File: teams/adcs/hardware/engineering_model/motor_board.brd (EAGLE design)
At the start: 90 x 90 mm, 63 parts

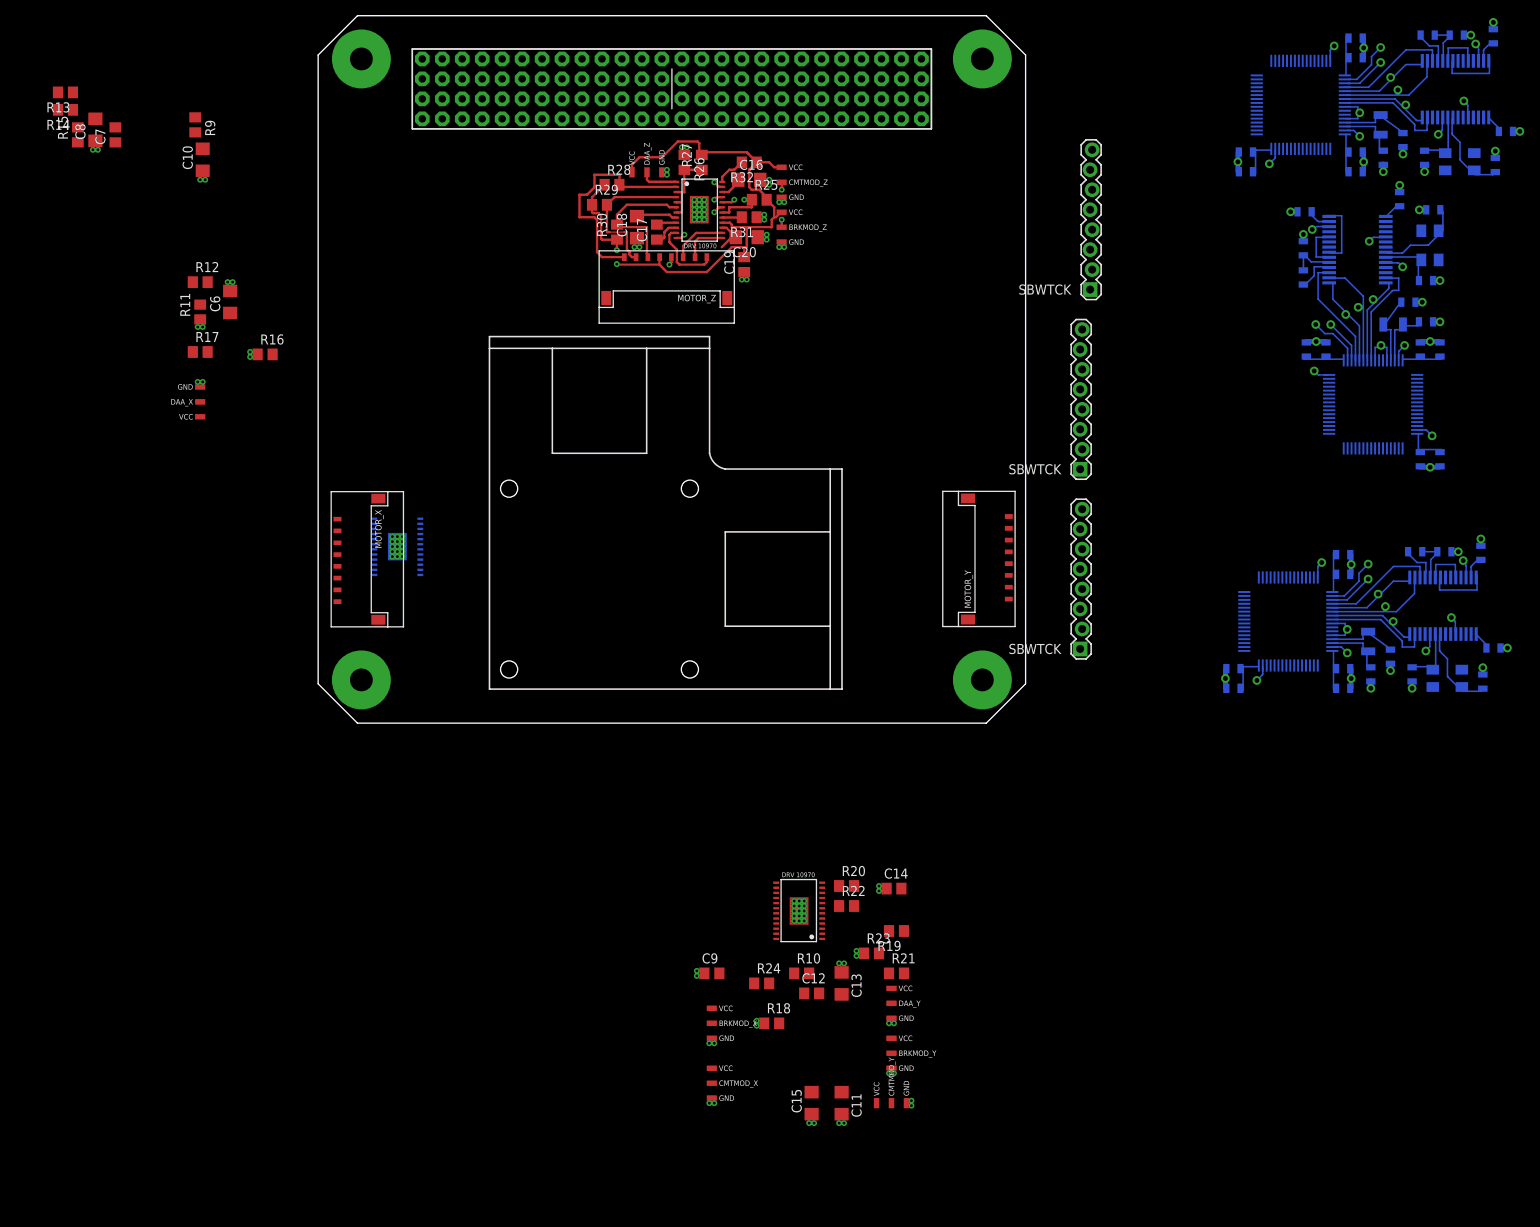
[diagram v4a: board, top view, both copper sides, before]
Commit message: ADCS/RW: Utilize design block in further routing progress
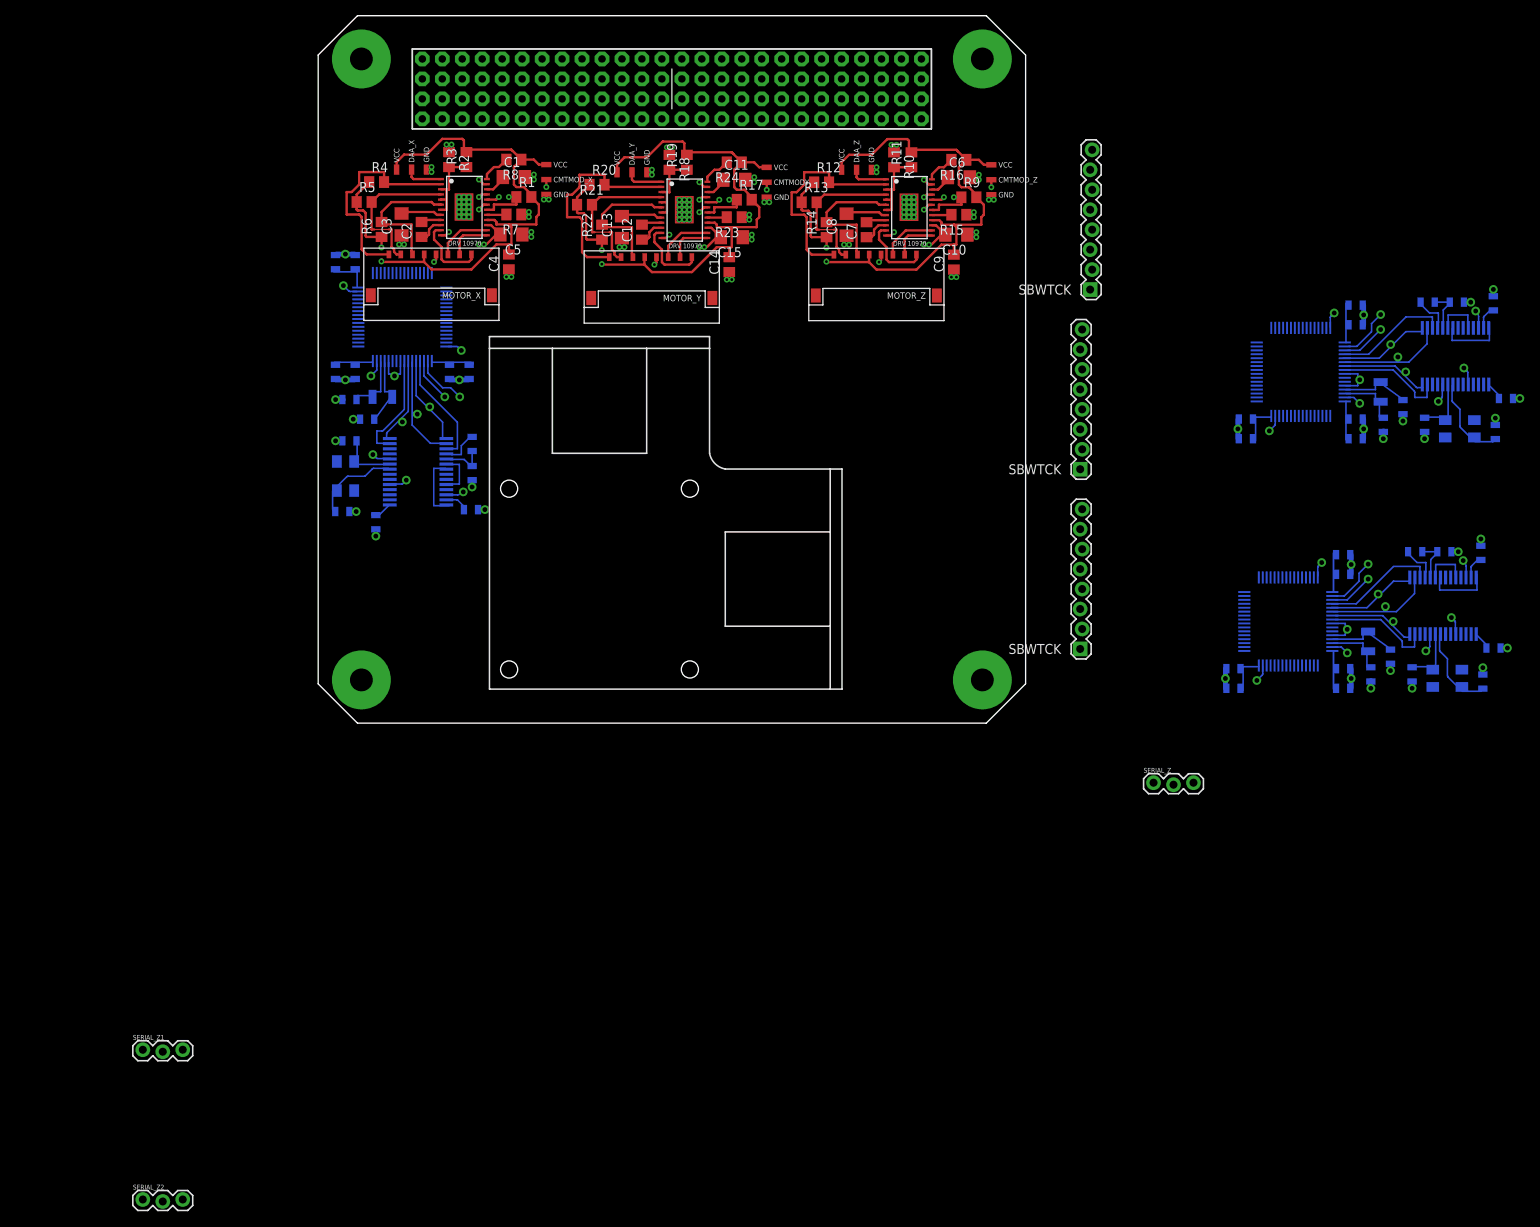
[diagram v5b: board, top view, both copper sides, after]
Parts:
- removed BRKMOD_X, BRKMOD_Y, BRKMOD_Z, CMTMOD_Y: 0_OHM_JUMPER, DubSat1 Components:0_OHM_JUMPER
- removed C16: 2.2uF, rcl:C1206
- removed C17, C19: 0.1uF, rcl:C0805
- removed C18, C20: 1uF, rcl:C1206
- removed R25, R26, R27, R32: 3.3K, rcl:R0805
- removed R28, R29, R30: 10K, rcl:R0805
- removed R31: (no value), rcl:R0805
- removed U$12: DRV10970, DubSat1 Components:DRV10970
- added C1: 2.2uF, rcl:C1206
- added C2, C4: 0.1uF, rcl:C0805
- added C3, C5: 1uF, rcl:C1206
- added CMTMODY: 0_OHM_JUMPER, DubSat1 Components:0_OHM_JUMPER
- added R1, R2, R3, R8: 3.3K, rcl:R0805
- added R4, R5, R6: 10K, rcl:R0805
- added R7: (no value), rcl:R0805
- added SERIAL_Z, SERIAL_Z1, SERIAL_Z2: (no value), SparkFun-Connectors:1X03_LOCK
- added U$13: DRV10970, DubSat1 Components:DRV10970
- R12: value 3.3K -> 10K
- R15: value 10K -> (none)
- R16: value (none) -> 3.3K
- moved C11 118.3 mm to (53.7, 69.8), turned to 0 degrees
- moved U$3 117.4 mm to (11.4, 52.4), turned to 180 degrees
- moved CMTMOD_X 116.9 mm to (29.7, 69.9)
- moved R15 112.5 mm to (82.2, 65.4), turned to 180 degrees
- moved DAA_Y 110.8 mm to (40.6, 70.8), turned to 90 degrees
- moved C15 110.6 mm to (53.3, 62.5), turned to 180 degrees
- moved R18 110.3 mm to (45.4, 72.1), turned to 270 degrees
- moved R21 105.5 mm to (34.6, 66.7)
- moved R24 104.5 mm to (53.7, 72.1), turned to 180 degrees
- moved R10 104.2 mm to (74.0, 72.4), turned to 270 degrees
- moved R19 101.4 mm to (47.6, 72.1), turned to 90 degrees
- moved C13 100.2 mm to (39.4, 63.8), turned to 90 degrees
- moved C12 99.2 mm to (41.9, 63.2), turned to 90 degrees
- moved U$7 99.2 mm to (19.3, 66.4), turned to 270 degrees
- moved R9 98.9 mm to (83.5, 67.6), turned to 0 degrees
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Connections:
- net N$20 renamed RETRY_Z
- net N$24 renamed VCP_Z
- net N$50 renamed CPP_Z
- net N$51 renamed CPN_Z
- removed net N$13: C11.1, U$7.RETRY
- removed net N$14: C13.2, U$7.VCP
- removed net N$15: R18.2, R19.1, U$7.U_HN, U$7.V_HN, U$7.W_HN
- removed net N$16: DAA_Y.P$2, U$7.DAA
- removed net N$17: CMTMOD_Y.P$2, U$7.CMTMOD
- removed net N$18: BRKMOD_Y.P$2, U$7.BRKMOD
- removed net N$21: C12.2, U$7.CPP
- removed net N$22: C12.1, U$7.CPN
- removed net N$23: MOTOR_Y.P$1, U$7.W
- removed net N$25: MOTOR_Y.P$2, U$7.V
- removed net N$30: R11.2, R12.1, U$10.U_HN, U$10.V_HN, U$10.W_HN
- removed net N$36: DAA_X.P$2, U$10.DAA
- removed net N$38: CMTMOD_X.P$2, U$10.CMTMOD
- removed net N$39: BRKMOD_X.P$2, U$10.BRKMOD
- removed net N$40: MOTOR_Y.P$6, R22.2, U$7.W_HP
- removed net N$41: MOTOR_Y.P$7, R21.2, U$7.V_HP
- removed net N$52: MOTOR_X.P$1, U$10.W
- removed net N$53: MOTOR_X.P$2, U$10.V
- removed net N$54: MOTOR_X.P$6, R15.2, U$10.W_HP
- removed net N$55: MOTOR_X.P$7, R14.2, U$10.V_HP
- removed net N$57: MOTOR_X.P$8, R13.2, U$10.U_HP
- removed net N$58: R16.2, U$10.CS
- removed net N$59: MOTOR_X.P$3, U$10.U
- removed net N$60: MOTOR_Y.P$8, R20.2, U$7.U_HP
- removed net N$61: R23.2, U$7.CS
- removed net N$62: MOTOR_Y.P$3, U$7.U
- removed net N$69: C16.1, U$12.RETRY
- removed net N$70: C18.2, U$12.VCP
- removed net N$71: R26.2, R27.1, U$12.U_HN, U$12.V_HN, U$12.W_HN
- removed net N$72: DAA_Z.P$2, U$12.DAA
- removed net N$73: CMTMOD_Z.P$2, U$12.CMTMOD
- removed net N$74: BRKMOD_Z.P$2, U$12.BRKMOD
- removed net N$75: C17.2, U$12.CPP
- removed net N$76: C17.1, U$12.CPN
- removed net N$77: MOTOR_Z.P$1, U$12.W
- removed net N$78: MOTOR_Z.P$2, U$12.V
- removed net N$79: MOTOR_Z.P$6, R30.2, U$12.W_HP
- removed net N$80: MOTOR_Z.P$7, R29.2, U$12.V_HP
- removed net N$81: MOTOR_Z.P$8, R28.2, U$12.U_HP
- removed net N$82: R31.2, U$12.CS
- removed net N$83: MOTOR_Z.P$3, U$12.U
- removed net VM_X: C10.2, U$10.VM
- removed net VM_Y: C15.2, U$7.VM
- new net BRKMOD_X: U$7.BRKMOD
- new net BRKMOD_Y: U$13.BRKMOD
- new net BRKMOD_Z: U$10.BRKMOD
- new net CMTMOD_X: CMTMOD_X.P$2, U$7.CMTMOD
- new net CMTMOD_Y: CMTMODY.P$2, U$13.CMTMOD
- new net CMTMOD_Z: CMTMOD_Z.P$2, U$10.CMTMOD
- new net CPN_X: C2.1, U$7.CPN
- new net CPN_Y: C12.1, U$13.CPN
- new net CPP_X: C2.2, U$7.CPP
- new net CPP_Y: C12.2, U$13.CPP
- new net CS_X: R7.2, U$7.CS
- new net CS_Y: R23.2, U$13.CS
- new net CS_Z: R15.2, U$10.CS
- new net DAA_X: DAA_X.P$2, U$7.DAA
- new net DAA_Y: DAA_Y.P$2, U$13.DAA
- new net DAA_Z: DAA_Z.P$2, U$10.DAA
- new net FG: U$8.P7.4_GPIO
- new net FR: U$8.P7.3_GPIO
- new net HN_X: R2.2, R3.1, U$7.U_HN, U$7.V_HN, U$7.W_HN
- new net HN_Y: R18.2, R19.1, U$13.U_HN, U$13.V_HN, U$13.W_HN
- new net HN_Z: R10.2, R11.1, U$10.U_HN, U$10.V_HN, U$10.W_HN
- new net HP_U_X: MOTOR_X.P$8, R4.2, U$7.U_HP
- new net HP_U_Y: MOTOR_Y.P$8, R20.2, U$13.U_HP
- new net HP_U_Z: MOTOR_Z.P$8, R12.2, U$10.U_HP
- new net HP_V_X: MOTOR_X.P$7, R5.2, U$7.V_HP
- new net HP_V_Y: MOTOR_Y.P$7, R21.2, U$13.V_HP
- new net HP_V_Z: MOTOR_Z.P$7, R13.2, U$10.V_HP
- new net HP_W_X: MOTOR_X.P$6, R6.2, U$7.W_HP
- new net HP_W_Y: MOTOR_Y.P$6, R22.2, U$13.W_HP
- new net HP_W_Z: MOTOR_Z.P$6, R14.2, U$10.W_HP
- new net M_Z_RX: SERIAL_Z.2, SERIAL_Z1.2, SERIAL_Z2.2, U$8.P2.6_GPIO/PWM
- new net M_Z_TX: SERIAL_Z.1, SERIAL_Z1.1, SERIAL_Z2.1, U$8.P2.5_GPIO
- new net PWM: U$8.P1.7_GPIO/PWM
- new net RD: U$8.P4.0_GPIO
- new net RETRY_X: C1.1, U$7.RETRY
- new net RETRY_Z_Y: C11.1, U$13.RETRY
- new net U_X: MOTOR_X.P$3, U$7.U
- new net U_Y: MOTOR_Y.P$3, U$13.U
- new net U_Z: MOTOR_Z.P$3, U$10.U
- new net V1_Z: MOTOR_Z.P$2, U$10.V
- new net VCP_X: C3.2, U$7.VCP
- new net VCP_Y: C13.2, U$13.VCP
- new net VM: C15.2, C5.2, U$13.VM, U$7.VM
- new net V_X: MOTOR_X.P$2, U$7.V
- new net V_Y: MOTOR_Y.P$2, U$13.V
- new net W_X: MOTOR_X.P$1, U$7.W
- new net W_Y: MOTOR_Y.P$1, U$13.W
- new net W_Z: MOTOR_Z.P$1, U$10.W
- net FG_X: now also R8.2, U$7.FG; no longer R17.2, U$10.FG
- net FG_Y: now also U$13.FG; no longer U$7.FG
- net FG_Z: now also R16.2, U$10.FG; no longer R32.2, U$12.FG, U$8.P7.4_GPIO
- net FR_X: now also U$7.FR; no longer U$10.FR
- net FR_Y: now also U$13.FR; no longer U$7.FR
- net FR_Z: now also U$10.FR; no longer U$12.FR, U$8.P7.3_GPIO
- net GND: now also C1.2, C3.1, C4.1, C5.1, CMTMODY.P$1, R10.1, R15.1, R2.1, R7.1, SERIAL_Z.3, SERIAL_Z1.3, SERIAL_Z2.3, U$13.GND@1, U$13.GND@2; no longer BRKMOD_X.P$1, BRKMOD_Y.P$1, BRKMOD_Z.P$1, C16.2, C18.1, C19.1, C20.1, CMTMOD_Y.P$1, R11.1, R16.1, R26.1, R31.1, U$12.GND@1, U$12.GND@2
- net PWM_X: now also U$7.PWM; no longer U$10.PWM
- net PWM_Y: now also U$13.PWM; no longer U$7.PWM
- net PWM_Z: now also U$10.PWM; no longer U$12.PWM, U$8.P1.7_GPIO/PWM
- net RD_X: now also R1.1, U$7.RD; no longer R9.1, U$10.RD
- net RD_Y: now also R17.1, U$13.RD; no longer R10.1, U$7.RD
- net RD_Z: now also R9.1, U$10.RD; no longer R25.1, U$12.RD, U$8.P4.0_GPIO
- net VINT_X: now also C4.2, R1.2, R3.2, R4.1, R5.1, R6.1, R8.1, U$7.VINT; no longer BRKMOD_X.P$3, C9.2, R12.2, R13.1, R14.1, R15.1, R17.1, R9.2, U$10.VINT
- net VINT_Y: now also CMTMODY.P$3, R17.2, U$13.VINT; no longer BRKMOD_Y.P$3, CMTMOD_Y.P$3, R10.2, U$7.VINT
- net VINT_Z: now also C9.2, R11.2, R12.1, R13.1, R14.1, R16.1, R9.2, U$10.VINT; no longer BRKMOD_Z.P$3, C19.2, R25.2, R27.2, R28.1, R29.1, R30.1, R32.1, U$12.VINT
- net VM_Z: now also C10.2, U$10.VM; no longer C20.2, U$12.VM
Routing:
- net GND: track 2.26 -> 96.8 mm, vias 101 -> 99
- net VINT_Y: track 0.00 -> 78.4 mm, vias 0 -> 2
- net VINT_X: track 0.00 -> 78.4 mm, vias 0 -> 2
- net N$81: track 29.2 -> 0.00 mm
- net HP_U_Y: track 0.00 -> 28.6 mm
- net HP_U_X: track 0.00 -> 28.6 mm
- net HP_U_Z: track 0.00 -> 28.6 mm
- net N$80: track 19.2 -> 0.00 mm
- net HP_V_Y: track 0.00 -> 19.2 mm
- net HP_V_X: track 0.00 -> 19.2 mm
- net HP_V_Z: track 0.00 -> 19.2 mm
- net N$79: track 17.3 -> 0.00 mm
- net HP_W_Z: track 0.00 -> 17.3 mm
- net HP_W_Y: track 0.00 -> 17.3 mm
- net HP_W_X: track 0.00 -> 17.3 mm
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
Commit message: ADCS/RW: Further routing
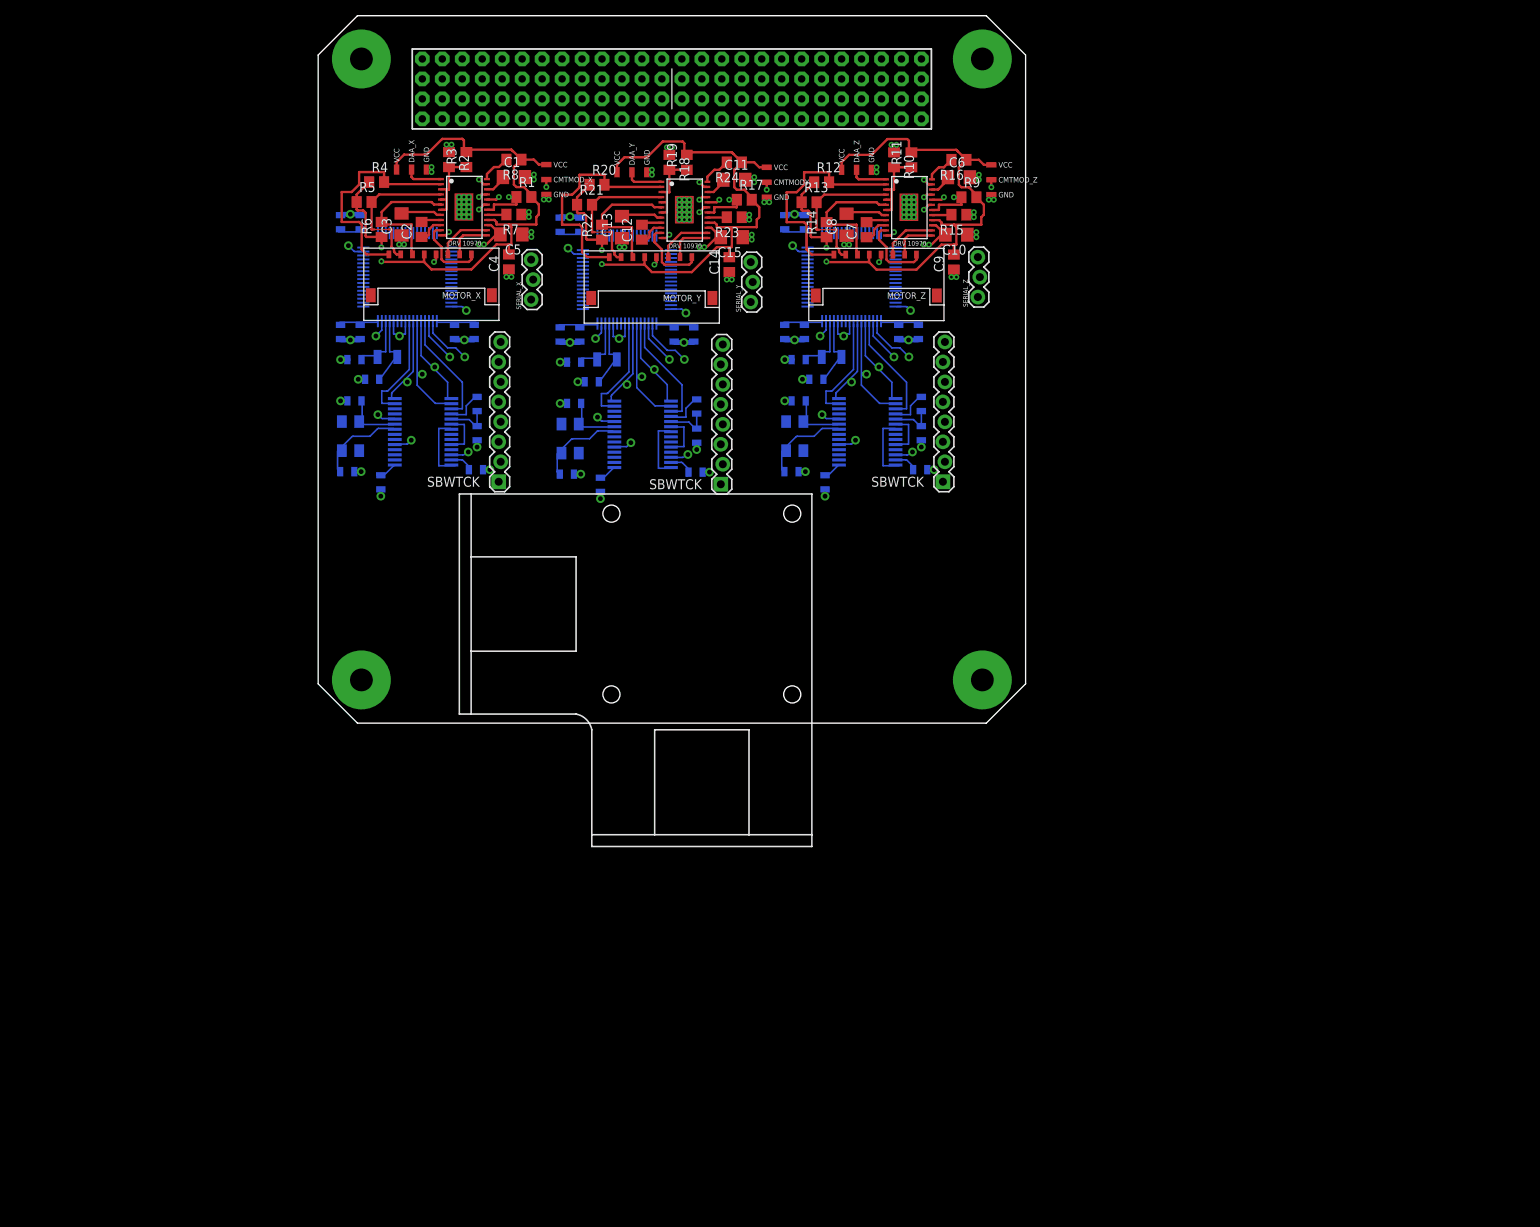
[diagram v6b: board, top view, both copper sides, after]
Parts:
- removed SERIAL_Z1, SERIAL_Z2: (no value), SparkFun-Connectors:1X03_LOCK
- added SERIAL_X, SERIAL_Y: (no value), SparkFun-Connectors:1X03_LOCK
- moved U$5 86.5 mm to (40.0, 57.1), turned to 180 degrees
- moved U$4 79.1 mm to (23.8, 31.4)
- moved U$8 70.8 mm to (68.6, 57.5), turned to 180 degrees
- moved SERIAL_Z 65.8 mm to (84.8, 54.9), turned to 90 degrees
- moved U$6 45.8 mm to (52.1, 31.1)
- moved U$11 27.5 mm to (80.3, 31.4)
- moved U$9 13.4 mm to (49.5, 15.9), turned to 180 degrees
- moved U$3 5.12 mm to (12.1, 57.5)
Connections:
- new net M_X_RX: SERIAL_X.2, U$3.P2.6_GPIO/PWM
- new net M_X_TX: SERIAL_X.1, U$3.P2.5_GPIO
- new net M_Y_RX: SERIAL_Y.2, U$5.P2.6_GPIO/PWM
- new net M_Y_TX: SERIAL_Y.1, U$5.P2.5_GPIO
- net GND: now also SERIAL_X.3, SERIAL_Y.3; no longer SERIAL_Z1.3, SERIAL_Z2.3
- net M_Z_RX: no longer SERIAL_Z1.2, SERIAL_Z2.2
- net M_Z_TX: no longer SERIAL_Z1.1, SERIAL_Z2.1
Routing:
- net HP_U_Y: track 28.6 -> 29.9 mm
- net HP_U_X: track 28.6 -> 29.9 mm
- net HP_U_Z: track 28.6 -> 29.9 mm

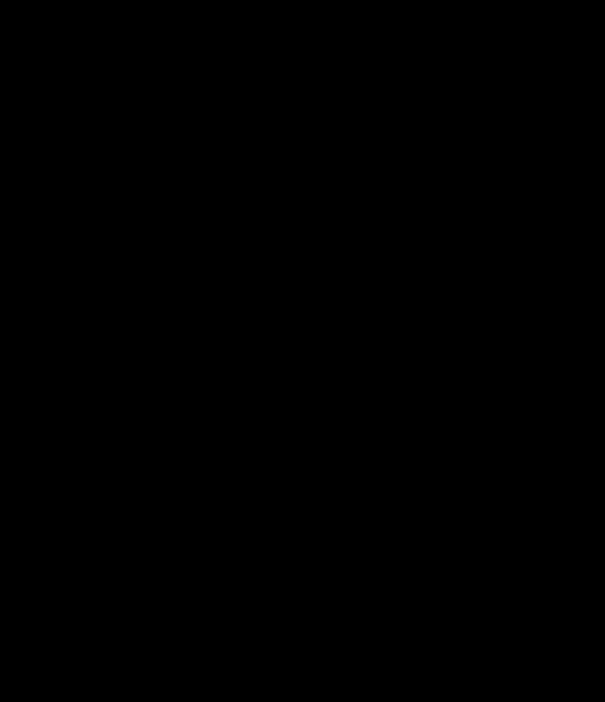
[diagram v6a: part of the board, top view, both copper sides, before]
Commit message: ADCS/RW: Added LDOs for microcontrollers
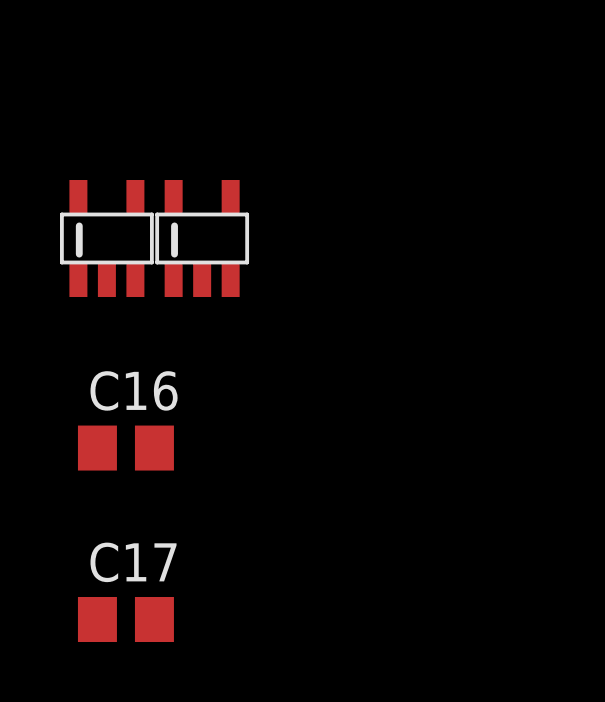
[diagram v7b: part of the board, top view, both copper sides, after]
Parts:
- added C16, C17: 0.01 μF, rcl:C0805
- added LDO_3V3, LDO_5V: LINEAR_LDO_LT1761-X, DubSat1 Components:SOT-23-5
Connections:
- new net N$13: C17.2, LDO_5V.P$4
- new net N$14: C16.2, LDO_3V3.P$4
- net +3V3: now also C16.1, LDO_3V3.P$5
- net +5V: now also C17.1, LDO_5V.P$5
- net GND: now also LDO_3V3.P$2, LDO_5V.P$2
- net VBAT: now also LDO_3V3.P$1, LDO_5V.P$1
